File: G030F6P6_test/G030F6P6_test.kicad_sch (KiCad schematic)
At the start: 36 parts, among them J1 Conn_01x10_Female, J2 Conn_01x02_Male, J3 Conn_01x10_Female, J4 USB_C_Receptacle_USB2.0, J5 Conn_01x05_Female, SW1 SW_Push_SPDT, U1 CH343P, U2 STM32G030FxP, U3 XC6206P332MR

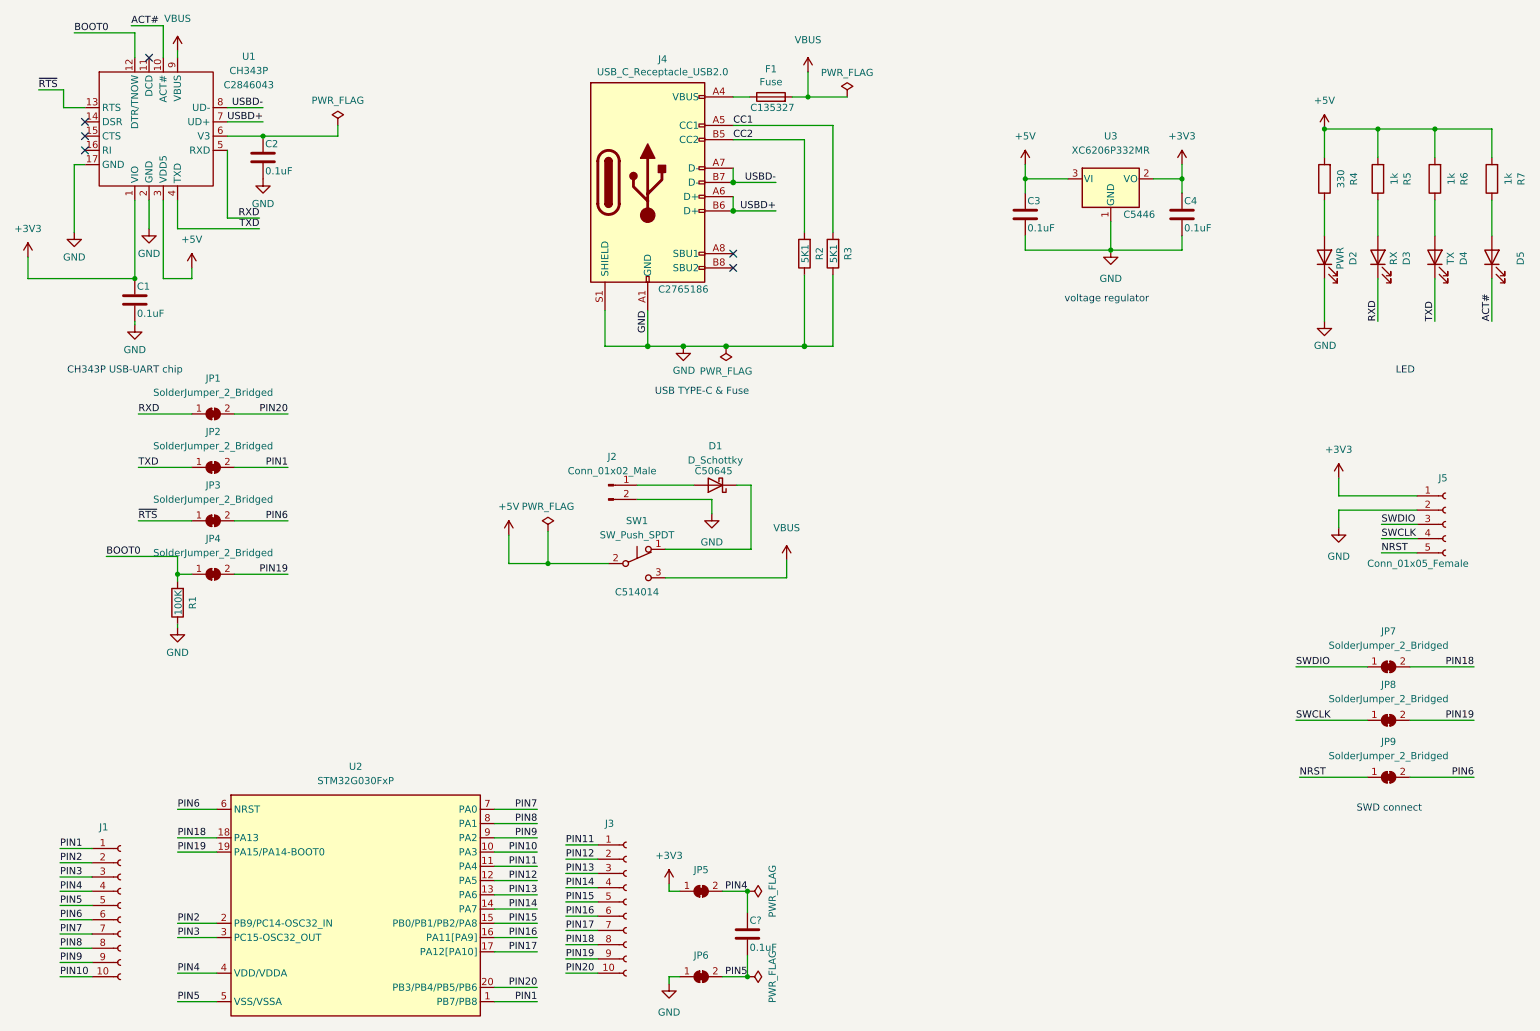
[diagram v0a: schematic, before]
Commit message: Update G030F6P6_test.kicad_sch
增加 LCSC 編號
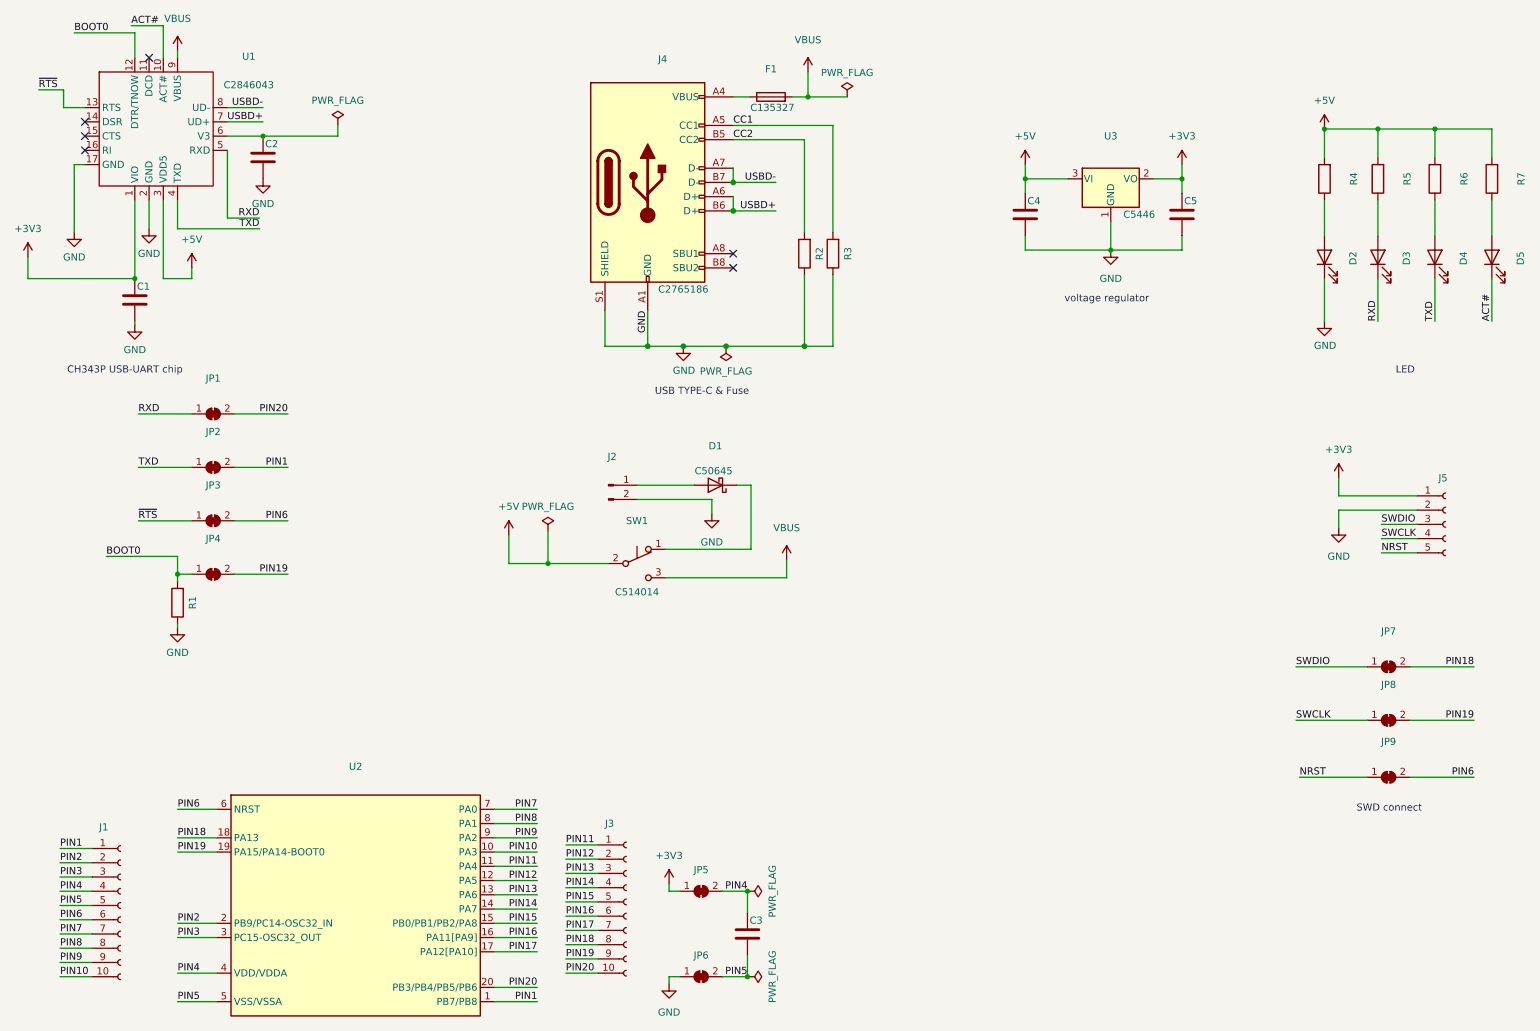
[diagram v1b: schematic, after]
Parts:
- C1, C2: value 0.1uF -> (none); footprint Capacitor_SMD:C_0805_2012Metric -> (none); LCSC (none) -> C1711
- C3: renamed from C?; value 0.1uF -> (none); footprint Capacitor_SMD:C_0805_2012Metric -> (none); LCSC (none) -> C1711
- C4: renamed from C3; value 0.1uF -> (none); footprint Capacitor_SMD:C_0805_2012Metric -> (none); LCSC (none) -> C1711
- C5: renamed from C4; value 0.1uF -> (none); footprint Capacitor_SMD:C_0805_2012Metric -> (none); LCSC (none) -> C1711
- D1: value D_Schottky -> (none); footprint Diode_SMD:D_SMA -> (none)
- D2: value PWR -> (none); footprint LED_SMD:LED_0805_2012Metric -> (none); LCSC (none) -> C72038
- D3: value RX -> (none); footprint LED_SMD:LED_0805_2012Metric -> (none); LCSC (none) -> C72043
- D4: value TX -> (none); footprint LED_SMD:LED_0805_2012Metric -> (none); LCSC (none) -> C84256
- D5: footprint LED_SMD:LED_0805_2012Metric -> (none); LCSC (none) -> C72038
- F1: value Fuse -> (none); footprint Fuse:Fuse_0805_2012Metric -> (none)
- J1, J3: value Conn_01x10_Female -> (none); footprint Connector_PinHeader_2.54mm:PinHeader_1x10_P2.54mm_Vertical -> (none)
- J2: value Conn_01x02_Male -> (none); footprint Connector_PinHeader_2.54mm:PinHeader_1x02_P2.54mm_Horizontal -> (none)
- J4: value USB_C_Receptacle_USB2.0 -> (none); footprint Connector_USB:USB_C_Receptacle_HRO_TYPE-C-31-M-12 -> (none)
- J5: value Conn_01x05_Female -> (none); footprint Connector_PinHeader_2.54mm:PinHeader_1x05_P2.54mm_Vertical -> (none)
- JP1, JP2, JP3, JP4, JP5, JP6, JP7, JP8, JP9: value SolderJumper_2_Bridged -> (none); footprint Jumper:SolderJumper-2_P1.3mm_Bridged2Bar_RoundedPad1.0x1.5mm -> (none)
- R1: value 100K -> (none); footprint Resistor_SMD:R_0805_2012Metric -> (none); LCSC (none) -> C149504
- R2, R3: value 5K1 -> (none); footprint Resistor_SMD:R_0805_2012Metric -> (none); LCSC (none) -> C27834
- R4: value 330 -> (none); footprint Resistor_SMD:R_0805_2012Metric -> (none); LCSC (none) -> C17630
- R5, R6, R7: value 1k -> (none); footprint Resistor_SMD:R_0805_2012Metric -> (none); LCSC (none) -> C25271
- SW1: value SW_Push_SPDT -> (none); footprint Button_Switch_SMD:SW_SPDT_PCM12 -> (none)
- U1: value CH343P -> (none); footprint Package_DFN_QFN:QFN-16-1EP_3x3mm_P0.5mm_EP1.45x1.45mm -> (none)
- U2: value STM32G030FxP -> (none); footprint Package_SO:TSSOP-20_4.4x6.5mm_P0.65mm -> (none); LCSC (none) -> C529330
- U3: value XC6206P332MR -> (none); footprint Package_TO_SOT_SMD:SOT-23 -> (none)

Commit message: Update G030F6P6_test.kicad_sch
更新CH343P 符號
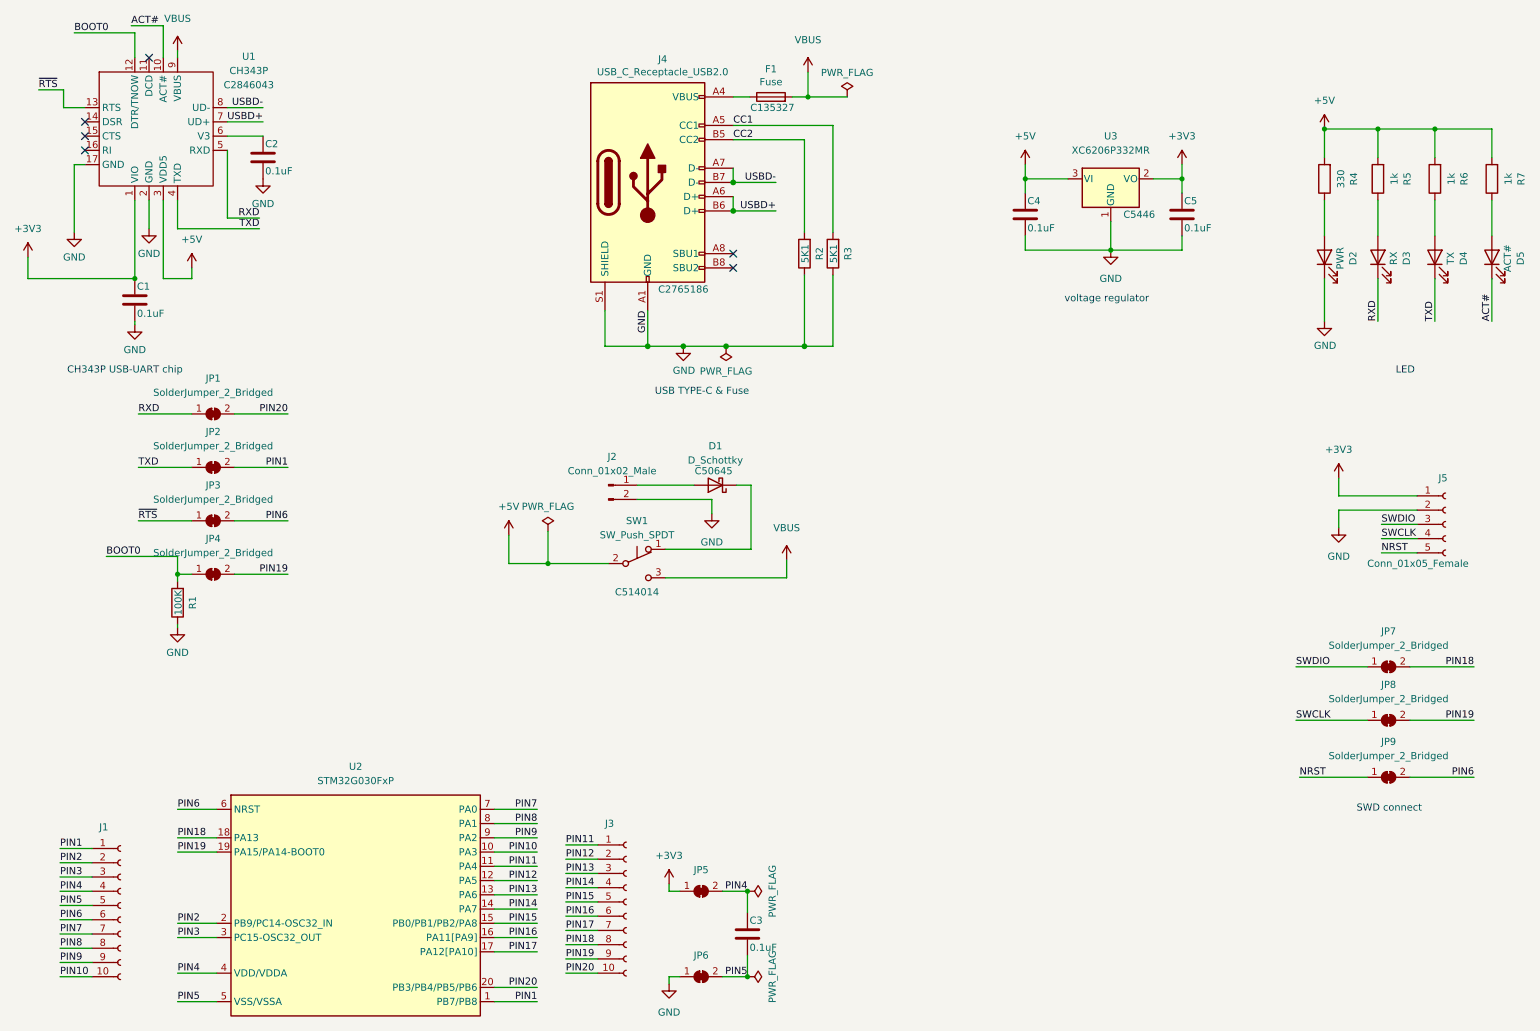
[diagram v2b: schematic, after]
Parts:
- C1, C2, C3, C4, C5: value (none) -> 0.1uF; footprint (none) -> Capacitor_SMD:C_0805_2012Metric
- D1: value (none) -> D_Schottky; footprint (none) -> Diode_SMD:D_SMA
- D2: value (none) -> PWR; footprint (none) -> LED_SMD:LED_0805_2012Metric
- D3: value (none) -> RX; footprint (none) -> LED_SMD:LED_0805_2012Metric
- D4: value (none) -> TX; footprint (none) -> LED_SMD:LED_0805_2012Metric
- D5: value (none) -> ACT#; footprint (none) -> LED_SMD:LED_0805_2012Metric
- F1: value (none) -> Fuse; footprint (none) -> Fuse:Fuse_0805_2012Metric
- J1, J3: value (none) -> Conn_01x10_Female; footprint (none) -> Connector_PinHeader_2.54mm:PinHeader_1x10_P2.54mm_Vertical
- J2: value (none) -> Conn_01x02_Male; footprint (none) -> Connector_PinHeader_2.54mm:PinHeader_1x02_P2.54mm_Horizontal
- J4: value (none) -> USB_C_Receptacle_USB2.0; footprint (none) -> Connector_USB:USB_C_Receptacle_HRO_TYPE-C-31-M-12
- J5: value (none) -> Conn_01x05_Female; footprint (none) -> Connector_PinHeader_2.54mm:PinHeader_1x05_P2.54mm_Vertical
- JP1, JP2, JP3, JP4, JP5, JP6, JP7, JP8, JP9: value (none) -> SolderJumper_2_Bridged; footprint (none) -> Jumper:SolderJumper-2_P1.3mm_Bridged2Bar_RoundedPad1.0x1.5mm
- R1: value (none) -> 100K; footprint (none) -> Resistor_SMD:R_0805_2012Metric
- R2, R3: value (none) -> 5K1; footprint (none) -> Resistor_SMD:R_0805_2012Metric
- R4: value (none) -> 330; footprint (none) -> Resistor_SMD:R_0805_2012Metric
- R5, R6, R7: value (none) -> 1k; footprint (none) -> Resistor_SMD:R_0805_2012Metric
- SW1: value (none) -> SW_Push_SPDT; footprint (none) -> Button_Switch_SMD:SW_SPDT_PCM12
- U1: value (none) -> CH343P; footprint (none) -> Package_DFN_QFN:QFN-16-1EP_3x3mm_P0.5mm_EP1.45x1.45mm
- U2: value (none) -> STM32G030FxP; footprint (none) -> Package_SO:TSSOP-20_4.4x6.5mm_P0.65mm
- U3: value (none) -> XC6206P332MR; footprint (none) -> Package_TO_SOT_SMD:SOT-23

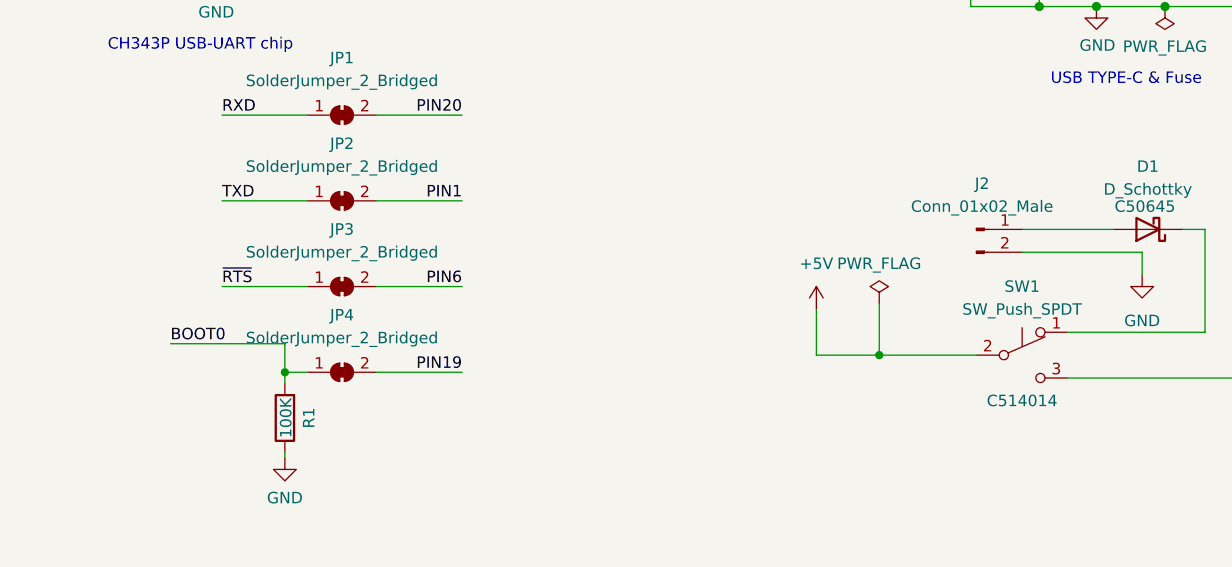
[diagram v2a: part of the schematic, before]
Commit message: Update G030F6P6_test.kicad_sch
修改 JP2 封裝
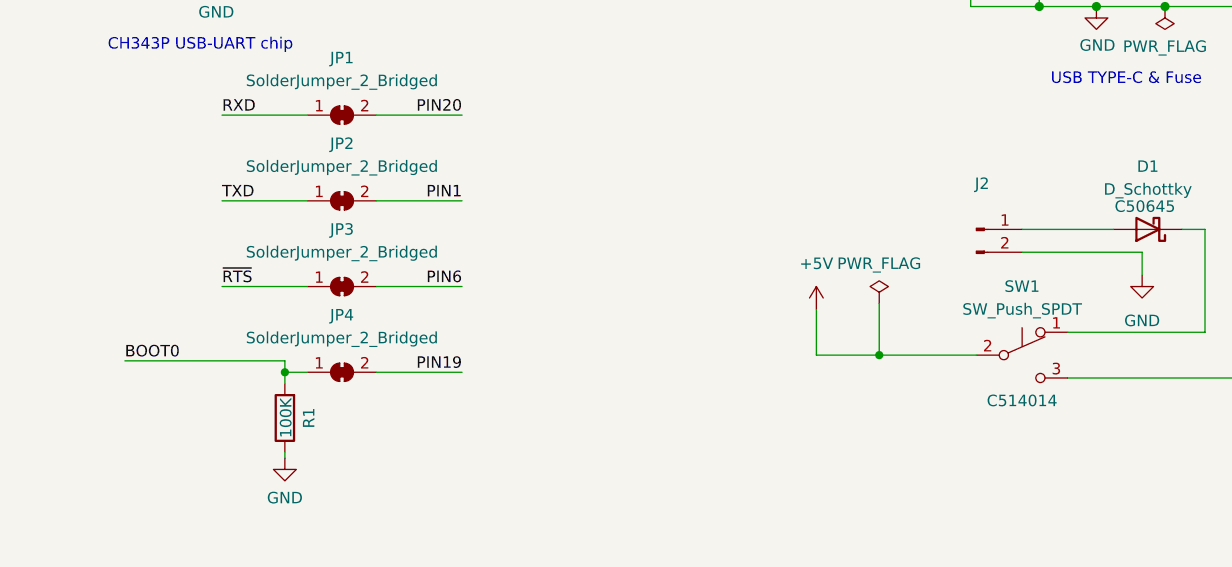
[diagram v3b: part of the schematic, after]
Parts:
- J2: value Conn_01x02_Male -> (none); footprint Connector_PinHeader_2.54mm:PinHeader_1x02_P2.54mm_Horizontal -> (none)
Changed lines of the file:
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@@
     (stroke (width 0) (type default) (color 0 0 0 0))
   )
-  (wire (pts (xy 44.45 111.76) (xy 44.45 114.935))
+  (wire (pts (xy 44.45 113.665) (xy 44.45 114.935))
     (stroke (width 0) (type default) (color 0 0 0 0))
   )
@@
     (stroke (width 0) (type default) (color 0 0 0 0))
   )
-  (wire (pts (xy 31.75 111.76) (xy 44.45 111.76))
+  (wire (pts (xy 26.67 113.665) (xy 44.45 113.665))
     (stroke (width 0) (type default) (color 0 0 0 0))
   )
@@
     (effects (font (size 1.27 1.27)) (justify right bottom))
   )
-  (label "BOOT0" (at 31.75 111.76 0)
+  (label "BOOT0" (at 26.67 113.665 0)
     (effects (font (size 1.27 1.27)) (justify left bottom))
   )
@@
     (in_bom yes) (on_board yes) (fields_autoplaced)
     (property "Reference" "J2" (id 0) (at 121.92 93.98 0))
-    (property "Value" "Conn_01x02_Male" (id 1) (at 121.92 96.52 0))
-    (property "Footprint" "Connector_PinHeader_2.54mm:PinHeader_1x02_P2.54mm_Horizontal" (id 2) (at 121.285 99.06 0)
+    (property "Value" "" (id 1) (at 121.92 96.52 0))
+    (property "Footprint" "" (id 2) (at 121.285 99.06 0)
       (effects (font (size 1.27 1.27)) hide)
     )
@@
     )
     (path "/745fe90e-c09f-4980-939d-c86bb79f5d7c"
-      (reference "J2") (unit 1) (value "Conn_01x02_Male") (footprint "Connector_PinHeader_2.54mm:PinHeader_1x02_P2.54mm_Horizontal")
+      (reference "J2") (unit 1) (value "Conn_01x02_Male") (footprint "Connector_PinHeader_2.54mm:PinHeader_1x02_P2.54mm_Vertical")
     )
     (path "/dea68bd7-448e-4645-961d-024e3f8df3a0"
